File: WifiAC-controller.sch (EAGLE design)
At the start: 10 parts

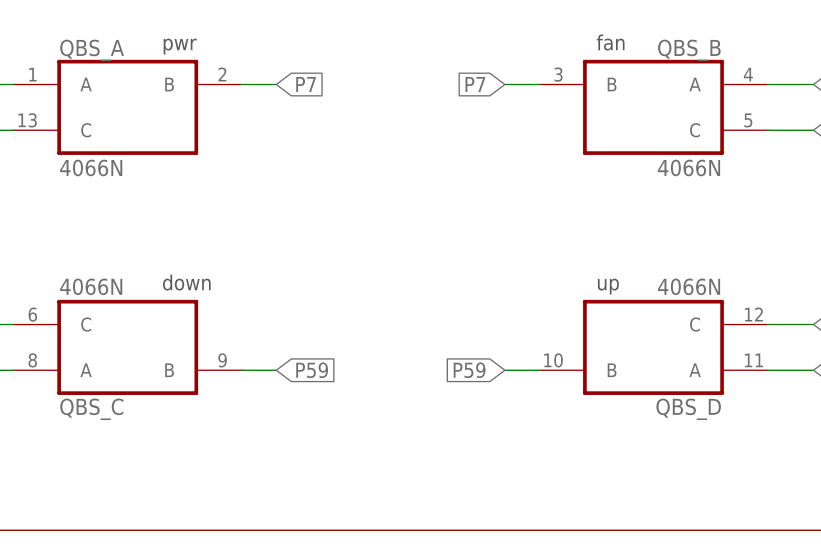
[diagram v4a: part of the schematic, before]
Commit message: fixed gpio numbering, some more coding
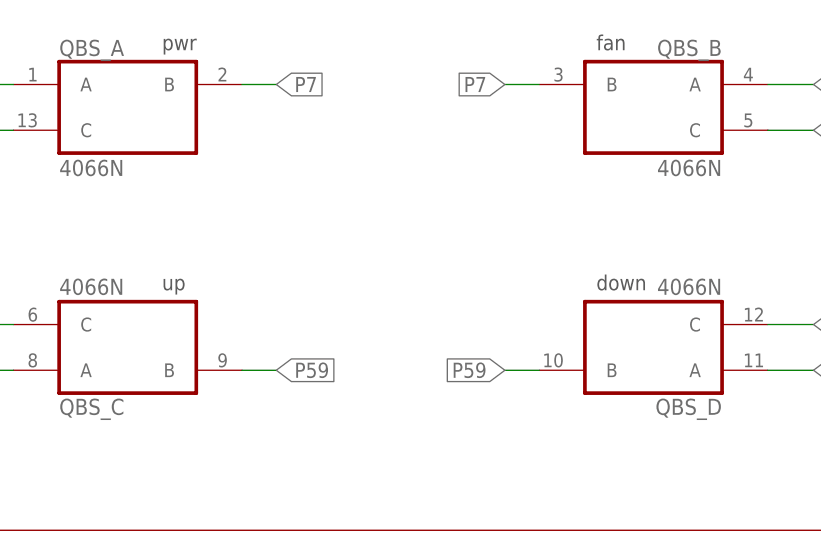
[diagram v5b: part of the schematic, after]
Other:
- note added: "down -> GPIO14"
- note added: "up -> GPIO13"
- note removed: "down -> GPIO13"
- note removed: "up -> GPIO14"
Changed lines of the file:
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@@
 <text x="176.53" y="88.9" size="1.6764" layer="97">pwr</text>
 <text x="224.79" y="88.9" size="1.6764" layer="97">fan</text>
-<text x="224.79" y="62.23" size="1.6764" layer="97">up</text>
-<text x="176.53" y="62.23" size="1.6764" layer="97">down</text>
+<text x="224.79" y="62.23" size="1.6764" layer="97">down</text>
+<text x="176.53" y="62.23" size="1.6764" layer="97">up</text>
 <wire x1="0" y1="96.52" x2="71.12" y2="96.52" width="0.1524" layer="94"/>
 <wire x1="71.12" y1="96.52" x2="85.09" y2="96.52" width="0.1524" layer="94"/>
@@
 <text x="228.6" y="128.27" size="2.54" layer="114">pwr -&gt; GPIO16</text>
 <text x="228.6" y="123.19" size="2.54" layer="114">fan -&gt; GPIO12</text>
-<text x="228.6" y="118.11" size="2.54" layer="114">down -&gt; GPIO13</text>
-<text x="228.6" y="113.03" size="2.54" layer="114">up -&gt; GPIO14</text>
+<text x="228.6" y="118.11" size="2.54" layer="114">up -&gt; GPIO13</text>
+<text x="228.6" y="113.03" size="2.54" layer="114">down -&gt; GPIO14</text>
 <text x="226.06" y="99.06" size="3.81" layer="97" font="vector">Pins_config</text>
 <text x="228.6" y="167.64" size="3.81" layer="114">INPUT PINS</text>

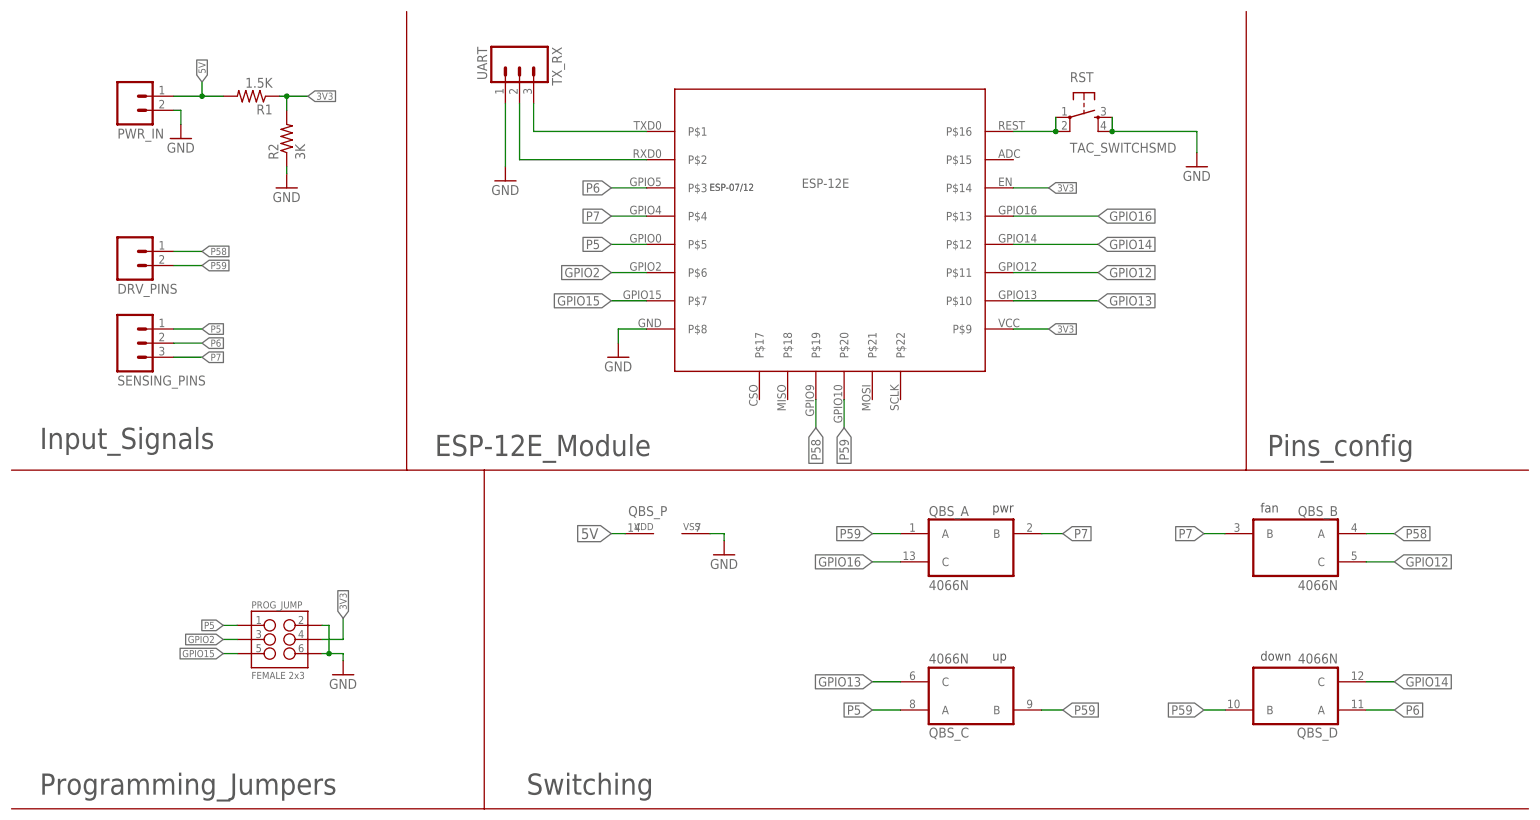
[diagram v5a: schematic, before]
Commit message: major fixes, changed the esp foot print, changed the connections, changed power supply, made the layout smaller
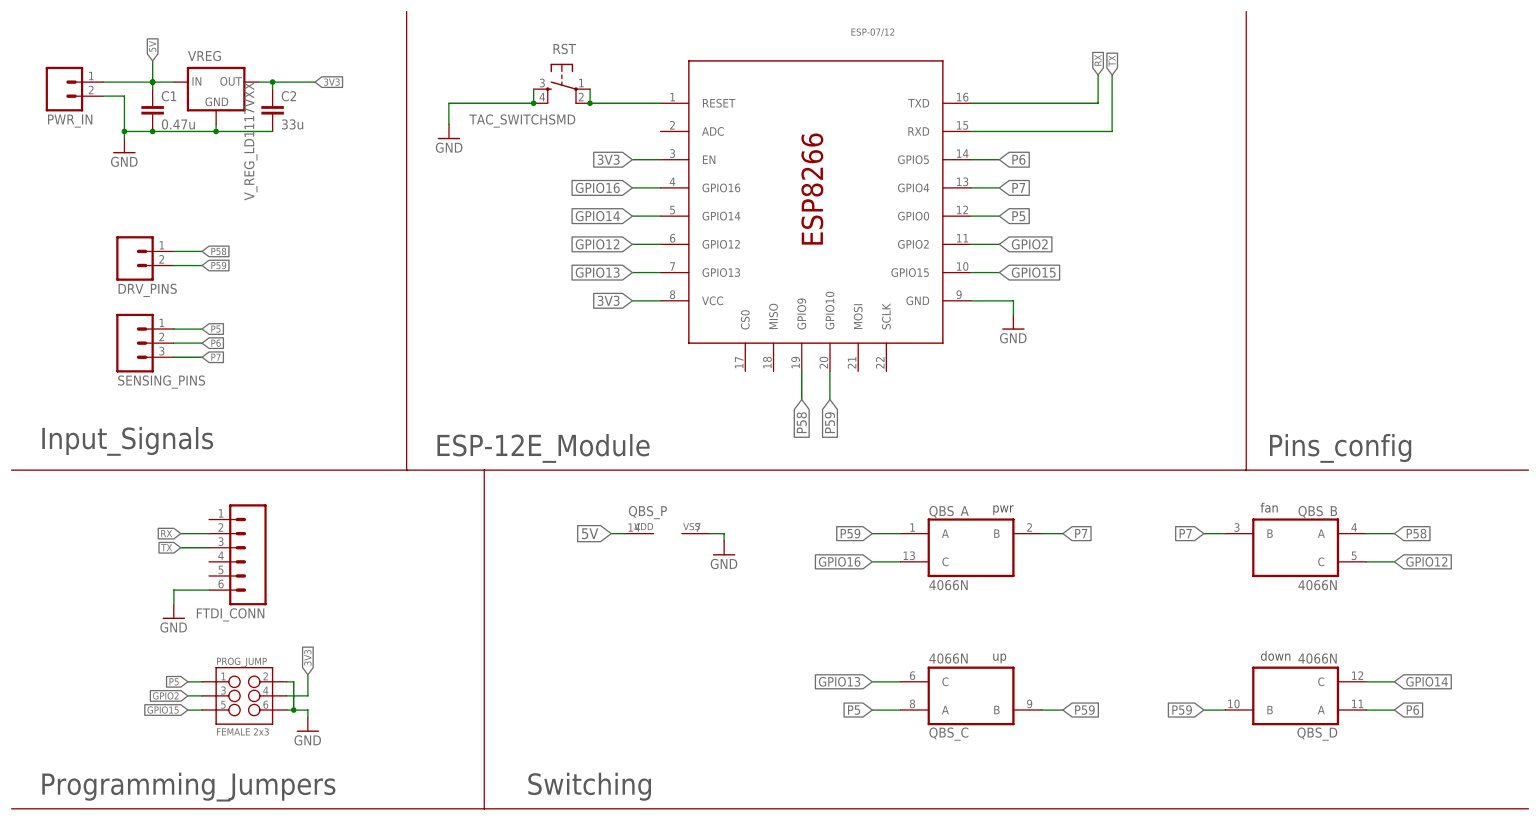
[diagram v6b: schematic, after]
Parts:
- removed R1: 1.5K, SparkFun-Resistors:RESISTOR1206
- removed R2: 3K, SparkFun-Resistors:RESISTORPTH-1/4W
- removed TX_RX: UART, SparkFun-Connectors:M03LONGPADS
- added C1: 0.47u, SparkFun-Passives:CAP1210
- added C2: 33u, SparkFun-Passives:CAP1210
- added FTDI_CONN: (no value), SparkFun-Connectors:M06NO_SILK_FEMALE_PTH
- added VREG: V_REG_LD1117VXX, SparkFun-PowerIC:V_REG_LD1117VXX
- ESP-12E: value ESP-07/12_ESP-12E -> ESP-07/12; device ESP-12E:ESP-07/12_ESP-12E -> ESP-12E:ESP-07/12
- SENSING_PINS: device SparkFun-Connectors:M03LONGPADS -> SparkFun-Connectors:M03PTH
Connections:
- removed net N$3: ESP-12E.P$1, TX_RX.3
- removed net N$4: ESP-12E.P$2, TX_RX.2
- new net RX: ESP-12E.TXD, FTDI_CONN.2
- new net TX: ESP-12E.RXD, FTDI_CONN.3
- net 3V3: now also C2.1, ESP-12E.EN, ESP-12E.VCC, VREG.OUT; no longer ESP-12E.P$14, ESP-12E.P$9, R1.1, R2.2
- net 5V: now also C1.1, VREG.IN; no longer R1.2
- net GND: now also C1.2, C2.2, ESP-12E.GND, FTDI_CONN.6, VREG.GND; no longer ESP-12E.P$8, R2.1, TX_RX.1
- net GPIO12: now also ESP-12E.GPIO12; no longer ESP-12E.P$11
- net GPIO13: now also ESP-12E.GPIO13; no longer ESP-12E.P$10
- net GPIO14: now also ESP-12E.GPIO14; no longer ESP-12E.P$12
- net GPIO15: now also ESP-12E.GPIO15; no longer ESP-12E.P$7
- net GPIO16: now also ESP-12E.GPIO16; no longer ESP-12E.P$13
- net GPIO2: now also ESP-12E.GPIO2; no longer ESP-12E.P$6
- net N$1: now also ESP-12E.RESET; no longer ESP-12E.P$16
- net P5: now also ESP-12E.GPIO0; no longer ESP-12E.P$5
- net P58: now also ESP-12E.GPIO9; no longer ESP-12E.P$19
- net P59: now also ESP-12E.GPIO10; no longer ESP-12E.P$20
- net P6: now also ESP-12E.GPIO5; no longer ESP-12E.P$3
- net P7: now also ESP-12E.GPIO4; no longer ESP-12E.P$4
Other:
- moved on the sheet: PROG_JUMP, PWR_IN, RST

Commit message: changed the smd capacitors to through hole
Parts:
- C1: device SparkFun-Passives:CAP1210 -> SparkFun-Passives:CAPEZ
- C2: device SparkFun-Passives:CAP1210 -> SparkFun-Passives:CAPPTH2
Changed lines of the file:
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@@
 <?xml version="1.0" encoding="utf-8"?>
 <!DOCTYPE eagle SYSTEM "eagle.dtd">
-<eagle version="7.3.0">
+<eagle version="7.4.0">
 <drawing>
 <settings>
@@
 <part name="GND7" library="SparkFun-Aesthetics" deviceset="GND" device=""/>
 <part name="VREG" library="SparkFun-PowerIC" deviceset="V_REG_LD1117VXX" device=""/>
-<part name="C1" library="SparkFun-Passives" deviceset="CAP" device="1210" value="0.47u"/>
-<part name="C2" library="SparkFun-Passives" deviceset="CAP" device="1210" value="33u"/>
+<part name="C1" library="SparkFun-Passives" deviceset="CAP" device="EZ" value="0.47u"/>
+<part name="C2" library="SparkFun-Passives" deviceset="CAP" device="PTH2" value="33u"/>
 <part name="FTDI_CONN" library="SparkFun-Connectors" deviceset="M06" device="NO_SILK_FEMALE_PTH"/>
 <part name="GND1" library="SparkFun-Aesthetics" deviceset="GND" device=""/>

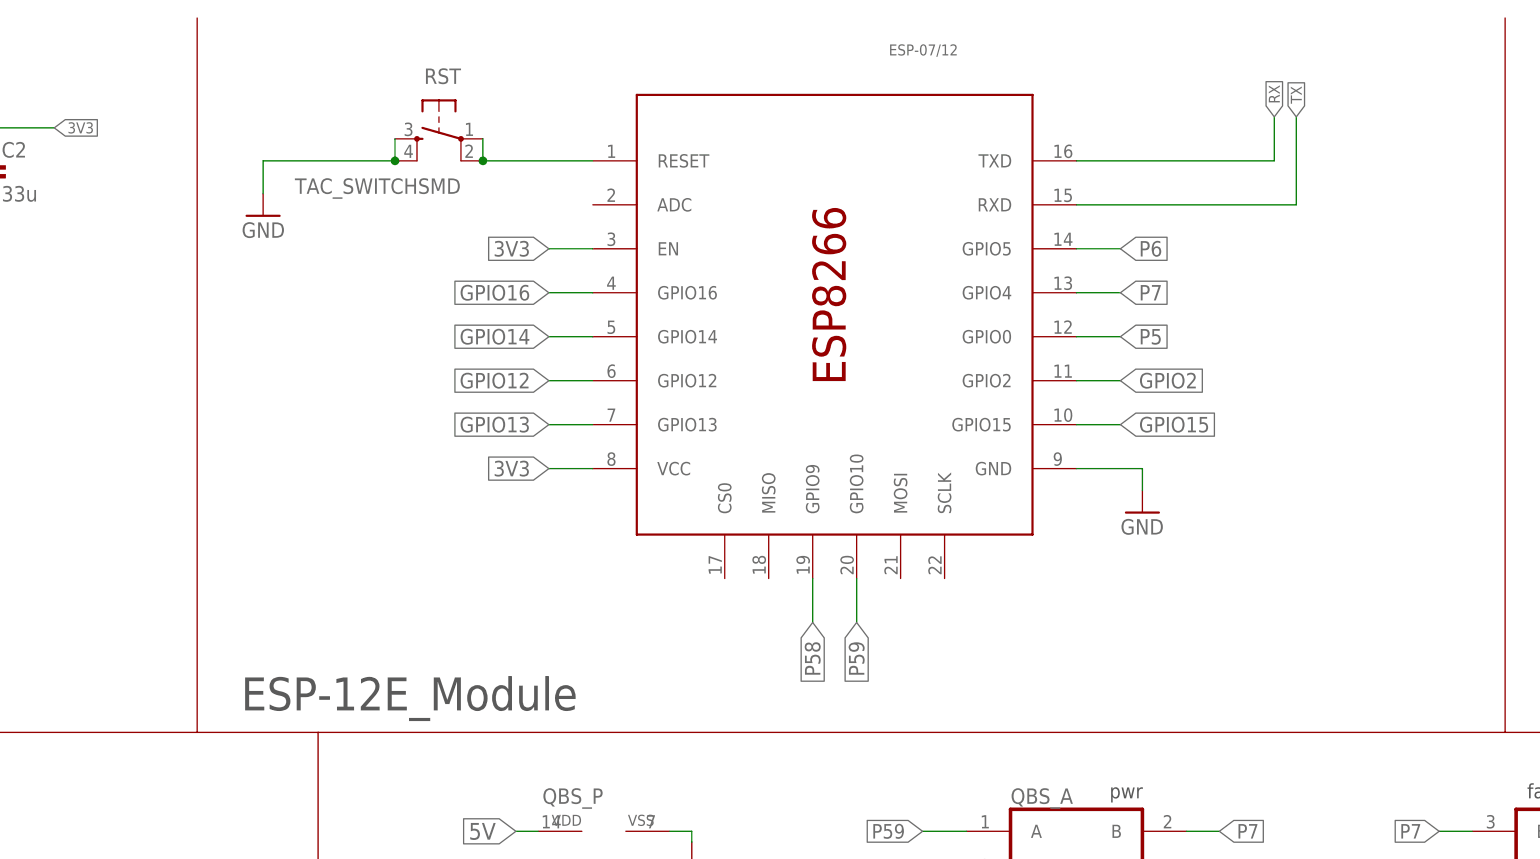
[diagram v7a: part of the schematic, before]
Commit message: changing to generic esp but the circuit is not done
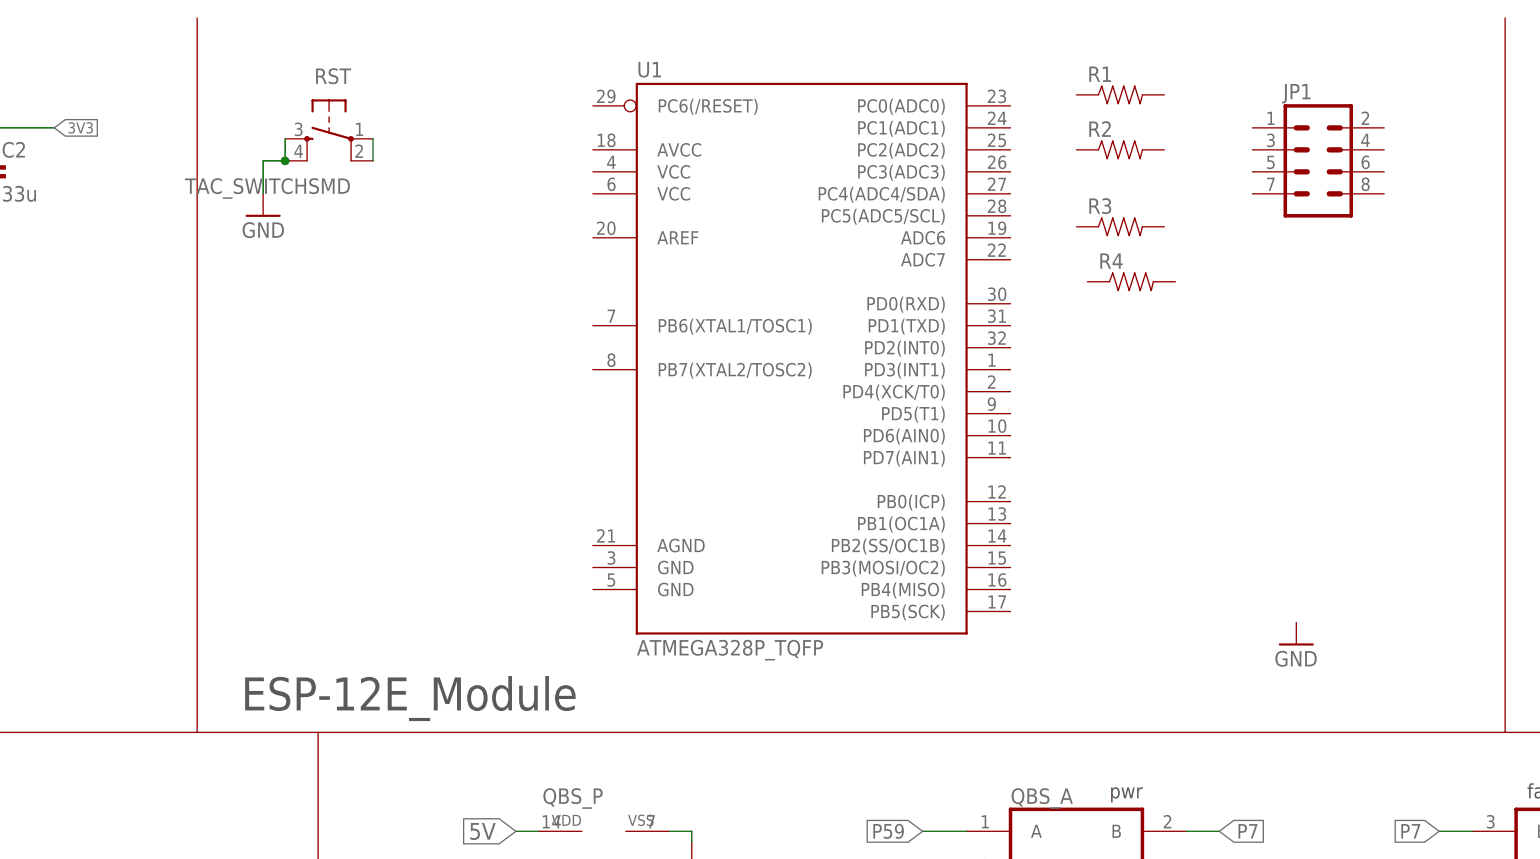
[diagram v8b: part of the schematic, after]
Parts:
- removed ESP-12E: ESP-07/12, ESP-12E:ESP-07/12
- added JP1: (no value), SparkFun-Connectors:M04X2
- added R1, R2, R3, R4: (no value), SparkFun-Passives:RESISTOR0805-RES
- added U1: ATMEGA328P_TQFP, SparkFun-DigitalIC:ATMEGA328P_TQFP
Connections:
- net 3V3: no longer ESP-12E.EN, ESP-12E.VCC
- net GND: no longer ESP-12E.GND
- net GPIO12: no longer ESP-12E.GPIO12
- net GPIO13: no longer ESP-12E.GPIO13
- net GPIO14: no longer ESP-12E.GPIO14
- net GPIO15: no longer ESP-12E.GPIO15
- net GPIO16: no longer ESP-12E.GPIO16
- net GPIO2: no longer ESP-12E.GPIO2
- net N$1: no longer ESP-12E.RESET
- net P5: no longer ESP-12E.GPIO0
- net P58: no longer ESP-12E.GPIO9
- net P59: no longer ESP-12E.GPIO10
- net P6: no longer ESP-12E.GPIO5
- net P7: no longer ESP-12E.GPIO4
- net RX: no longer ESP-12E.TXD
- net TX: no longer ESP-12E.RXD
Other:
- moved on the sheet: RST
